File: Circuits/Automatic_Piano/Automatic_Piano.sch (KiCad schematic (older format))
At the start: 0 parts

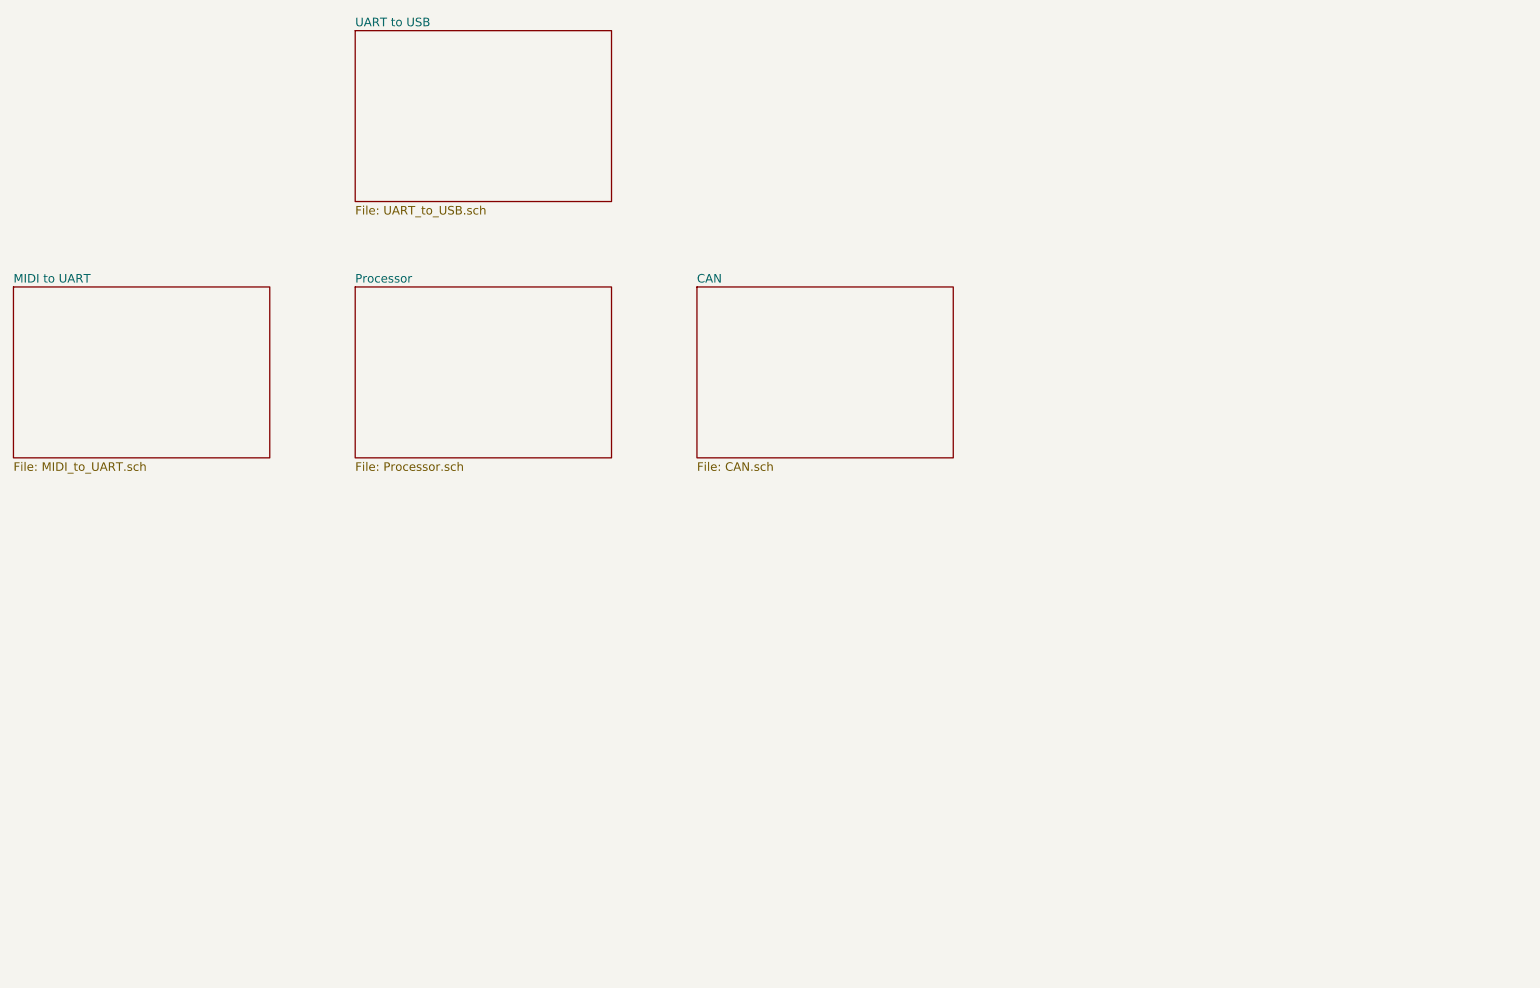
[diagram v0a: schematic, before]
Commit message: Completed MIDI to UART and UART to USB. Needs referencing
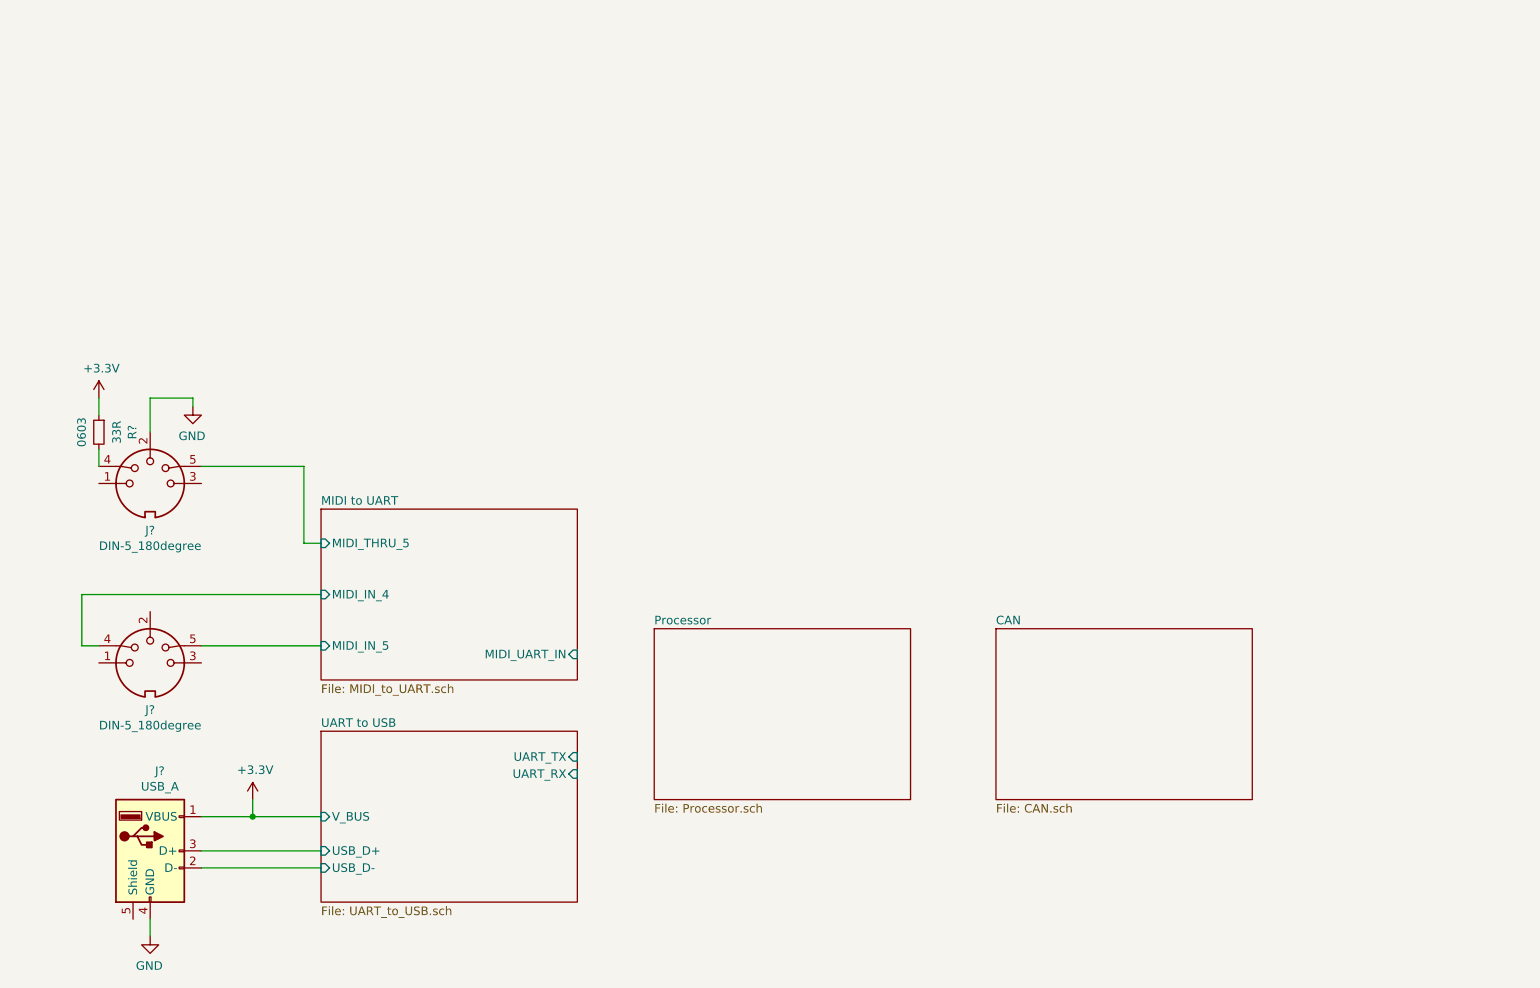
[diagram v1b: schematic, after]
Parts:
- added J? (x2): DIN-5_180degree, symbol Connector:DIN-5_180degree
- added J?: USB_A, symbol Connector:USB_A
- added R?: 33R, Resistor_SMD:R_0603_1608Metric, symbol Device:R_Small
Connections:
- new net: J?.4, R?.2
- new net +3V3: J?.1 (VBUS), R?.1
- new net GND: J?.2, J?.4 (GND)
- new net MIDI to UART/MIDI_IN_4: J?.4
- new net MIDI to UART/MIDI_IN_5: J?.5
- new net MIDI to UART/MIDI_THRU_5: J?.5
- new net UART to USB/USB_D+: J?.3 (D+)
- new net UART to USB/USB_D-: J?.2 (D-)
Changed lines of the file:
@@
 $EndDescr
 $Sheet
-S 1500 2500 1500 1000
+S 3300 3800 1500 1000
 U 5E18C714
 F0 "MIDI to UART" 50
 F1 "MIDI_to_UART.sch" 50
+F2 "MIDI_UART_IN" I R 4800 4650 50
+F3 "MIDI_IN_4" I L 3300 4300 50
+F4 "MIDI_IN_5" I L 3300 4600 50
+F5 "MIDI_THRU_5" I L 3300 4000 50
 $EndSheet
 $Sheet
-S 3500 2500 1500 1000
+S 5250 4500 1500 1000
 U 5E18CB51
 F0 "Processor" 50
@@
 $EndSheet
 $Sheet
-S 3500 1000 1500 1000
+S 3300 5100 1500 1000
 U 5E18D7E6
 F0 "UART to USB" 50
 F1 "UART_to_USB.sch" 50
+F2 "V_BUS" I L 3300 5600 50
+F3 "USB_D-" I L 3300 5900 50
+F4 "USB_D+" I L 3300 5800 50
+F5 "UART_TX" I R 4800 5250 50
+F6 "UART_RX" I R 4800 5350 50
 $EndSheet
 $Sheet
-S 5500 2500 1500 1000
+S 7250 4500 1500 1000
 U 5E18D8EB
 F0 "CAN" 50
 F1 "CAN.sch" 50
 $EndSheet
+$Comp
+L Connector:DIN-5_180degree J?
+U 1 1 5E1CF2E9
+P 2300 4700
+AR Path="/5E18C714/5E1CF2E9" Ref="J?"  Part="1"
+AR Path="/5E1CF2E9" Ref="J?"  Part="1"
+F 0 "J?" H 2300 4425 50  0000 C CNN
+F 1 "DIN-5_180degree" H 2300 4334 50  0000 C CNN
+F 2 "" H 2300 4700 50  0001 C CNN
+F 3 "http://www.mouser.com/ds/2/18/40_c091_abd_e-75918.pdf" H 2300 4700 50  0001 C CNN
+	1    2300 4700
+	1    0    0    -1
+$EndComp
+$Comp
+L Connector:DIN-5_180degree J?
+U 1 1 5E1F1711
+P 2300 3650
+AR Path="/5E18C714/5E1F1711" Ref="J?"  Part="1"
+AR Path="/5E1F1711" Ref="J?"  Part="1"
+F 0 "J?" H 2300 3375 50  0000 C CNN
+F 1 "DIN-5_180degree" H 2300 3284 50  0000 C CNN
+F 2 "" H 2300 3650 50  0001 C CNN
+F 3 "http://www.mouser.com/ds/2/18/40_c091_abd_e-75918.pdf" H 2300 3650 50  0001 C CNN
+	1    2300 3650
+	1    0    0    -1
+$EndComp
+$Comp
+L Device:R_Small R?
+U 1 1 5E1F171E
+P 2000 3350
+AR Path="/5E18C714/5E1F171E" Ref="R?"  Part="1"
+AR Path="/5E1F171E" Ref="R?"  Part="1"
+F 0 "R?" V 1804 3350 50  0000 C CNN
+F 1 "33R" V 1895 3350 50  0000 C CNN
+F 2 "Resistor_SMD:R_0603_1608Metric" H 2000 3350 50  0001 C CNN
+F 3 "~" H 2000 3350 50  0001 C CNN
+F 4 "0603" V 2100 3350 50  0000 C CNN "FootprintField"
+	1    2000 3350
+	-1   0    0    -1
+$EndComp
+Wire Wire Line
+	2000 3150 2000 3250
+Wire Wire Line
+	2000 3450 2000 3550
+$Comp
+L power:GND #PWR?
+U 1 1 5E1F1726
+P 2550 3200
+AR Path="/5E18C714/5E1F1726" Ref="#PWR?"  Part="1"
+AR Path="/5E1F1726" Ref="#PWR?"  Part="1"
+F 0 "#PWR?" H 2550 2950 50  0001 C CNN
+F 1 "GND" H 2555 3027 50  0000 C CNN
+F 2 "" H 2550 3200 50  0001 C CNN
+F 3 "" H 2550 3200 50  0001 C CNN
+	1    2550 3200
+	-1   0    0    -1
+$EndComp
+Wire Wire Line
+	2550 3150 2550 3200
+Wire Wire Line
+	2300 3350 2300 3150
+Wire Wire Line
+	2550 3150 2300 3150
+Wire Wire Line
+	2000 4600 1900 4600
+Wire Wire Line
+	1900 4600 1900 4300
+Wire Wire Line
+	1900 4300 3300 4300
+Wire Wire Line
+	2600 4600 3300 4600
+Wire Wire Line
+	2600 3550 3200 3550
+Wire Wire Line
+	3200 3550 3200 4000
+Wire Wire Line
+	3200 4000 3300 4000
+$Comp
+L power:+3.3V #PWR?
+U 1 1 5E200EC6
+P 2000 3150
+AR Path="/5E18C714/5E200EC6" Ref="#PWR?"  Part="1"
+AR Path="/5E200EC6" Ref="#PWR?"  Part="1"
+F 0 "#PWR?" H 2000 3000 50  0001 C CNN
+F 1 "+3.3V" H 2015 3323 50  0000 C CNN
+F 2 "" H 2000 3150 50  0001 C CNN
+F 3 "" H 2000 3150 50  0001 C CNN
+	1    2000 3150
+	1    0    0    -1
+$EndComp
+$Comp
+L Connector:USB_A J?
+U 1 1 5E21817D
+P 2300 5800
+F 0 "J?" H 2357 6267 50  0000 C CNN
+F 1 "USB_A" H 2357 6176 50  0000 C CNN
+F 2 "" H 2450 5750 50  0001 C CNN
+F 3 " ~" H 2450 5750 50  0001 C CNN
+	1    2300 5800
+	1    0    0    -1
+$EndComp
+Wire Wire Line
+	2600 5600 2900 5600
+Wire Wire Line
+	2600 5800 3300 5800
+Wire Wire Line
+	2600 5900 3300 5900
+$Comp
+L power:GND #PWR?
+U 1 1 5E2256B5
+P 2300 6300
+AR Path="/5E18C714/5E2256B5" Ref="#PWR?"  Part="1"
+AR Path="/5E2256B5" Ref="#PWR?"  Part="1"
+F 0 "#PWR?" H 2300 6050 50  0001 C CNN
+F 1 "GND" H 2305 6127 50  0000 C CNN
+F 2 "" H 2300 6300 50  0001 C CNN
+F 3 "" H 2300 6300 50  0001 C CNN
+	1    2300 6300
+	-1   0    0    -1
+$EndComp
+Wire Wire Line
+	2300 6200 2300 6300
+$Comp
+L power:+3.3V #PWR?
+U 1 1 5E22651E
+P 2900 5500
+AR Path="/5E18C714/5E22651E" Ref="#PWR?"  Part="1"
+AR Path="/5E22651E" Ref="#PWR?"  Part="1"
+F 0 "#PWR?" H 2900 5350 50  0001 C CNN
+F 1 "+3.3V" H 2915 5673 50  0000 C CNN
+F 2 "" H 2900 5500 50  0001 C CNN
+F 3 "" H 2900 5500 50  0001 C CNN
+	1    2900 5500
+	1    0    0    -1
+$EndComp
+Wire Wire Line
+	2900 5600 2900 5500
+Connection ~ 2900 5600
+Wire Wire Line
+	2900 5600 3300 5600
 $EndSCHEMATC

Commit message: Main Piano MIDI receiver completed. Might want indicator LEDS and more peripherals.
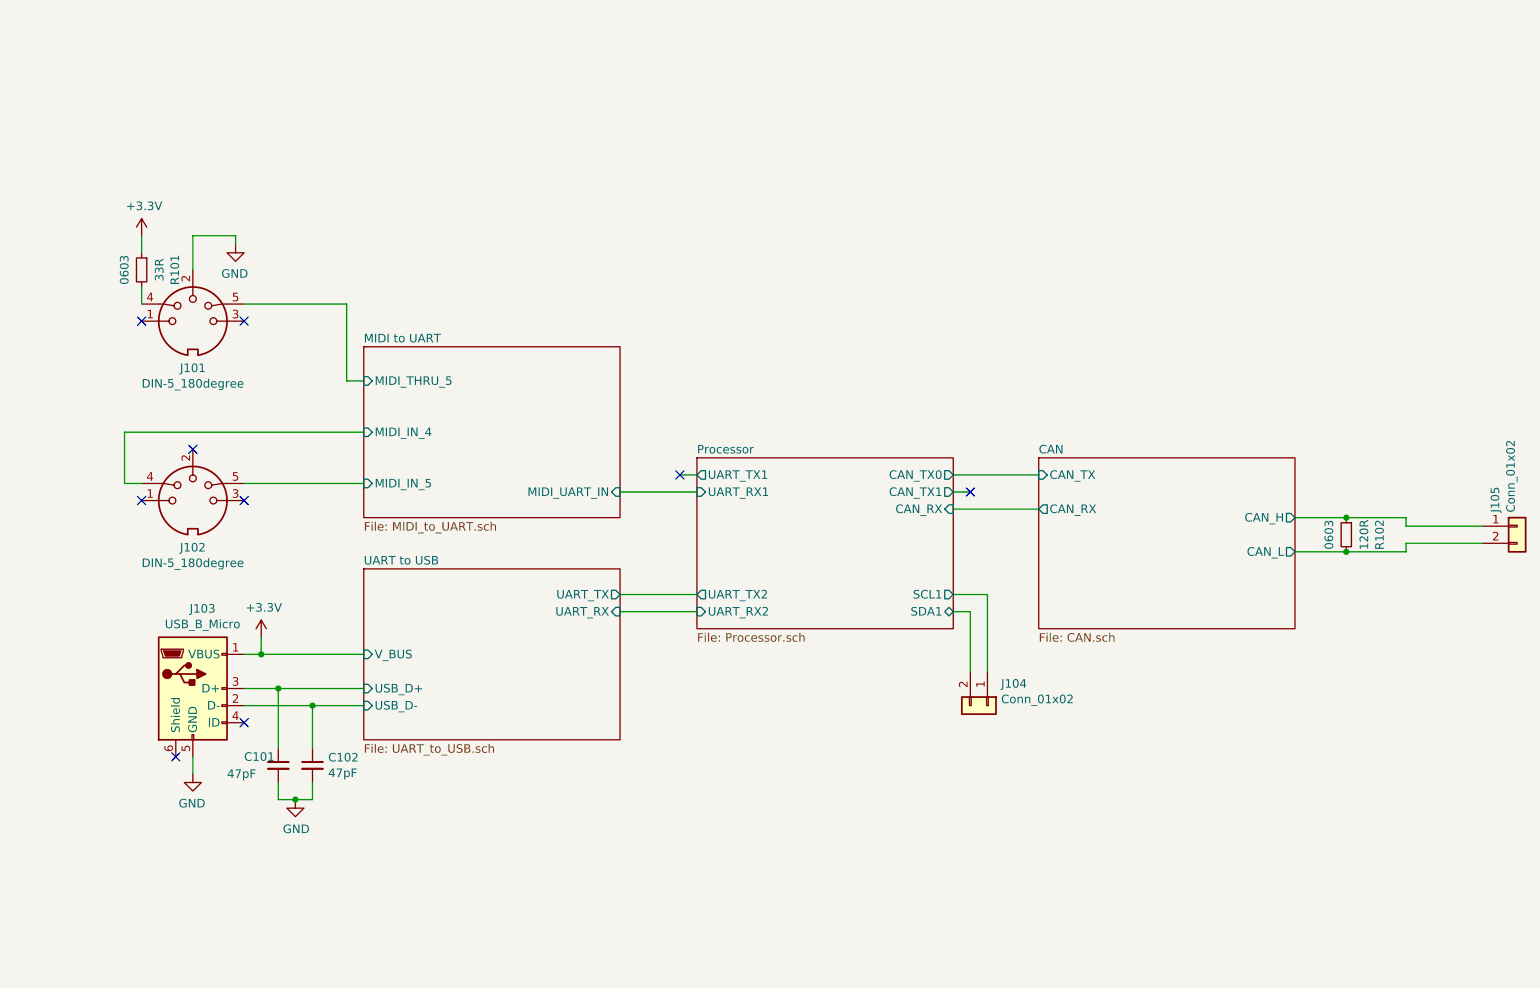
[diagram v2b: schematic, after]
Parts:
- removed J?: USB_A, symbol Connector:USB_A
- added C101, C102: 47pF, symbol Device:C_Small
- added J103: USB_B_Micro, symbol Connector:USB_B_Micro
- added J104, J105: Conn_01x02, symbol Connector_Generic:Conn_01x02
- added R102: 120R, Resistor_SMD:R_0603_1608Metric, symbol Device:R_Small
- gave numbers to parts that had none: 3
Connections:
- net +3V3: now also J103.1 (VBUS)
- net GND: now also C101.2, C102.2, J103.5 (GND)
- net UART to USB/USB_D+: now also C101.1, J103.3 (D+)
- net UART to USB/USB_D-: now also C102.1, J103.2 (D-)
- new net CAN/CAN_H: J105.1 (Pin_1), R102.1
- new net CAN/CAN_L: J105.2 (Pin_2), R102.2
- new net Processor/SCL1: J104.1 (Pin_1)
- new net Processor/SDA1: J104.2 (Pin_2)
- no-connect marks 0 -> 9
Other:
- moved on the sheet: J101, J102, R101
